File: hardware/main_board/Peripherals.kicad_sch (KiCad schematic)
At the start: 2 parts, among them J102 2x5 Socket Pins, J7 1x8 Male Pins

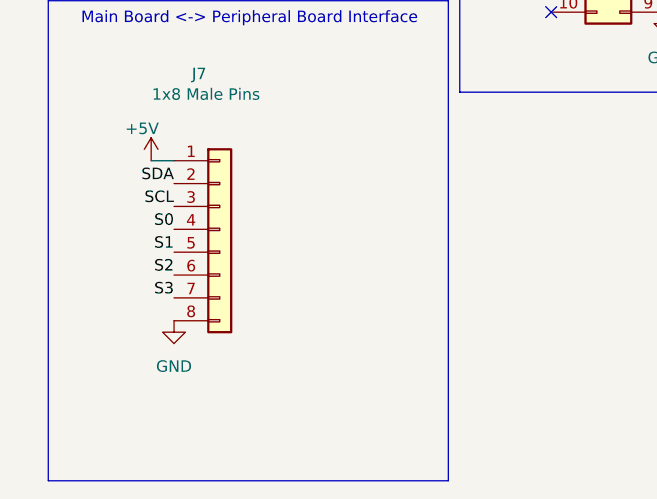
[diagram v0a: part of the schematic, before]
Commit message: added lakshay suggestions to peripheral board. removed bypass jumper from main board audio amp. added led strip interface. added too many things to remember i forgor
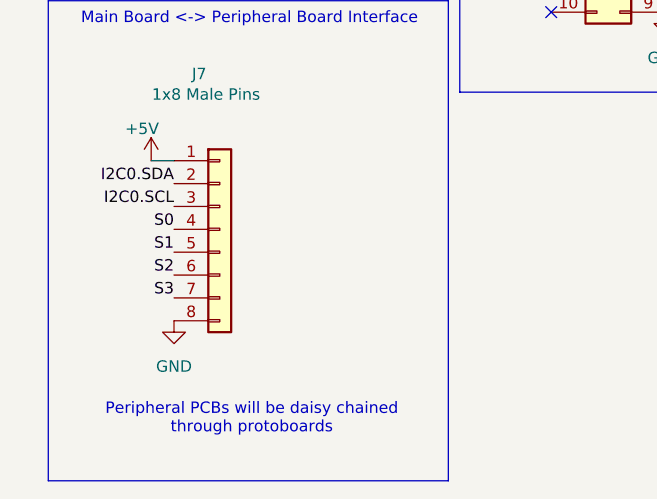
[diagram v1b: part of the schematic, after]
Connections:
- net SCL is gone; now on net I2C0.SCL: J7.3 (Pin_3)
- net SDA is gone; now on net I2C0.SDA: J7.2 (Pin_2)
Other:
- note added: "Peripheral PCBs will be daisy chained through protoboards"
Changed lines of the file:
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@@
+		)
+	)
+	(text "Peripheral PCBs will be daisy chained\nthrough protoboards"
+		(exclude_from_sim no)
+		(at 35.306 85.852 0)
+		(effects
+			(font
+				(size 1.27 1.27)
+			)
 		)
 	)
@@
 		)
 	)
-	(label "SDA"
-		(at 26.67 59.69 180)
+	(label "I2C0.SCL"
+		(at 26.67 62.23 180)
 		(effects
 			(font
@@
 		)
 	)
+	(label "I2C0.SDA"
+		(at 26.67 59.69 180)
+		(effects
+			(font
+				(size 1.27 1.27)
+			)
+			(justify right bottom)
+		)
+	)
 	(label "S0"
 		(at 27.94 24.13 0)
@@
 		(effects
 			(font
-				(size 1.27 1.27)
-			)
-			(justify right bottom)
-		)
-	)
-	(label "SCL"
-		(at 26.67 62.23 180)
-		(effects
-			(font
